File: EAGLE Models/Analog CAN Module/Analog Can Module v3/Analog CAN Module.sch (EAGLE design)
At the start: 241 parts, among them IC1 AT90CAN128, IC2 MCP2551SO8, IC3 NUP2105L, IC5 FT232RL, Q1 56P2859, U1 LTC2053, U10 LTC2053, U11 LTC2053, U12 LTC2053, U13 LTC2053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

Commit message: Added CC resistors
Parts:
- removed R12: (no value), rcl:R-US_R0603
- added R11, R84, R85, R86, R87, R88, R89, R90, R91, R92, R93, R94, R95, R96, R97, R98: (no value), rcl:R-US_R0603
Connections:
- new net A10CC: D17.C, R90.2
- new net A11CC: D18.C, R88.2
- new net A12CC: D11.C, R11.2
- new net A13CC: D12.C, R84.2
- new net A14CC: D13.C, R85.2
- new net A15CC: D14.C, R86.2
- new net A16CC: D15.C, R87.2
- new net A17CC: D26.C, R91.2
- new net A18CC: D25.C, R92.2
- new net A19CC: D23.C, R93.2
- new net A20CC: D24.C, R94.2
- new net A21CC: D19.C, R98.2
- new net A22CC: D20.C, R97.2
- new net A23CC: D21.C, R96.2
- new net A24CC: D22.C, R95.2
- new net A9CC: D16.C, R89.2
- net A10: now also R90.1; no longer D17.C
- net A11: now also R88.1; no longer D18.C
- net A12: now also R11.1; no longer D11.C
- net A13: now also R84.1; no longer D12.C
- net A14: now also R85.1; no longer D13.C
- net A15: now also R86.1; no longer D14.C
- net A16: now also R87.1; no longer D15.C
- net A17: now also R91.1; no longer D26.C
- net A18: now also R92.1; no longer D25.C
- net A19: now also R93.1; no longer D23.C
- net A20: now also R94.1; no longer D24.C
- net A21: now also R98.1; no longer D19.C
- net A22: now also R97.1; no longer D20.C
- net A23: now also R96.1; no longer D21.C
- net A24: now also R95.1; no longer D22.C
- net A8: no longer R12.1
- net A8CC: no longer R12.2
- net A9: now also R89.1; no longer D16.C
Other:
- moved on the sheet: D19

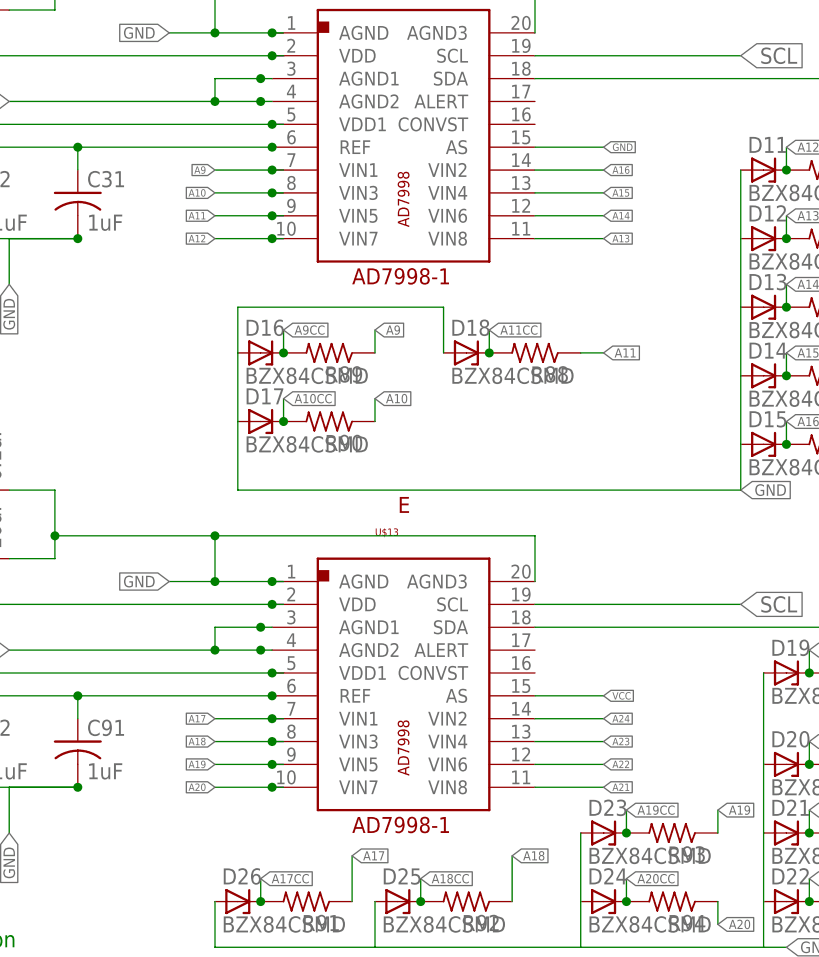
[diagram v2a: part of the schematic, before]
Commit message: Corrected ADC imputs
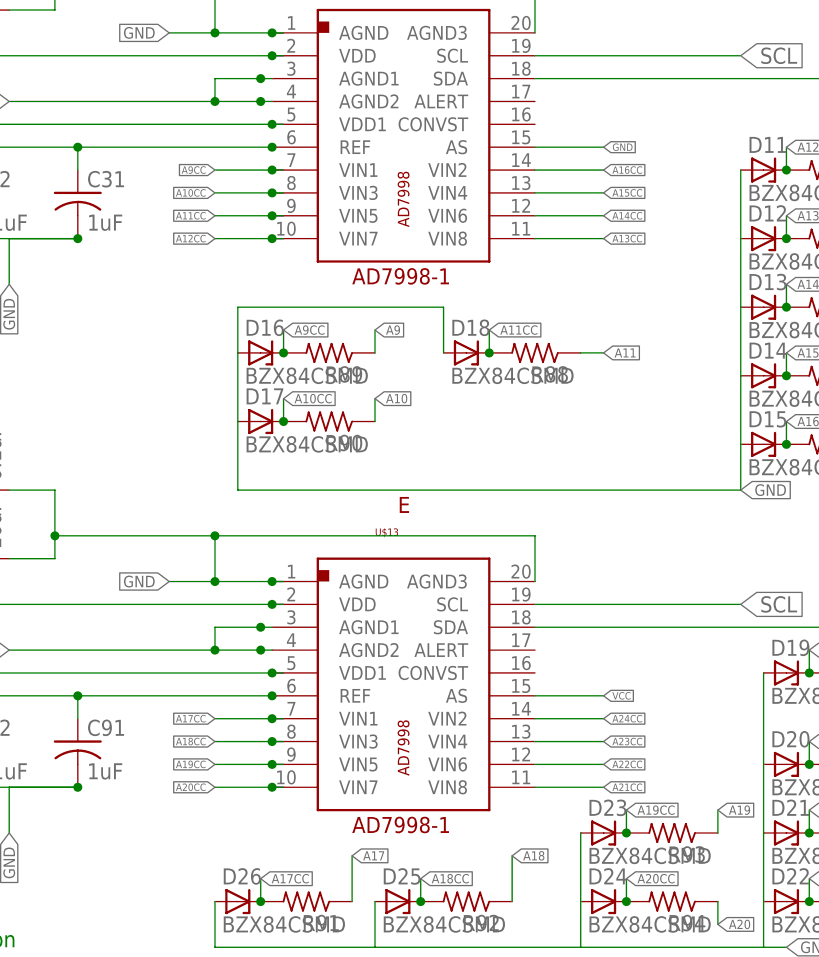
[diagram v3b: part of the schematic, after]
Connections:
- net A10: no longer U$9.VIN3
- net A10CC: now also U$9.VIN3
- net A11: no longer U$9.VIN5
- net A11CC: now also U$9.VIN5
- net A12: no longer U$9.VIN7
- net A12CC: now also U$9.VIN7
- net A13: no longer U$9.VIN8
- net A13CC: now also U$9.VIN8
- net A14: no longer U$9.VIN6
- net A14CC: now also U$9.VIN6
- net A15: no longer U$9.VIN4
- net A15CC: now also U$9.VIN4
- net A16: no longer U$9.VIN2
- net A16CC: now also U$9.VIN2
- net A17: no longer U$13.VIN1
- net A17CC: now also U$13.VIN1
- net A18: no longer U$13.VIN3
- net A18CC: now also U$13.VIN3
- net A19: no longer U$13.VIN5
- net A19CC: now also U$13.VIN5
- net A20: no longer U$13.VIN7
- net A20CC: now also U$13.VIN7
- net A21: no longer U$13.VIN8
- net A21CC: now also U$13.VIN8
- net A22: no longer U$13.VIN6
- net A22CC: now also U$13.VIN6
- net A23: no longer U$13.VIN4
- net A23CC: now also U$13.VIN4
- net A24: no longer U$13.VIN2
- net A24CC: now also U$13.VIN2
- net A9: no longer U$9.VIN1
- net A9CC: now also U$9.VIN1

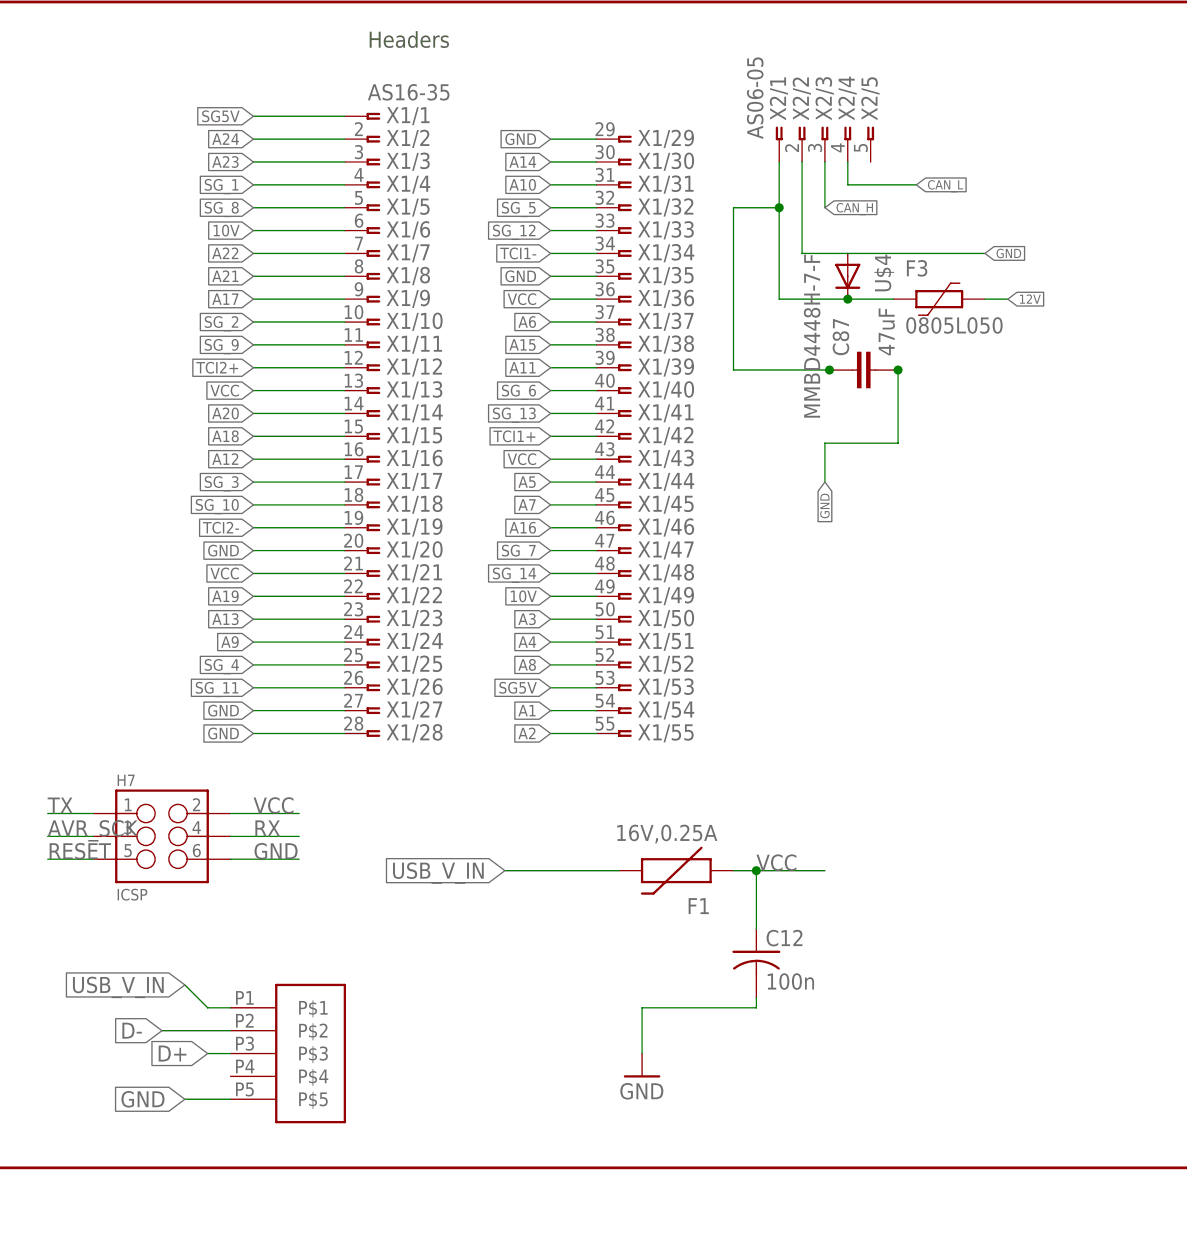
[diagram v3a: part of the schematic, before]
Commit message: Updated decoupling cap circuit, added more gnd vias
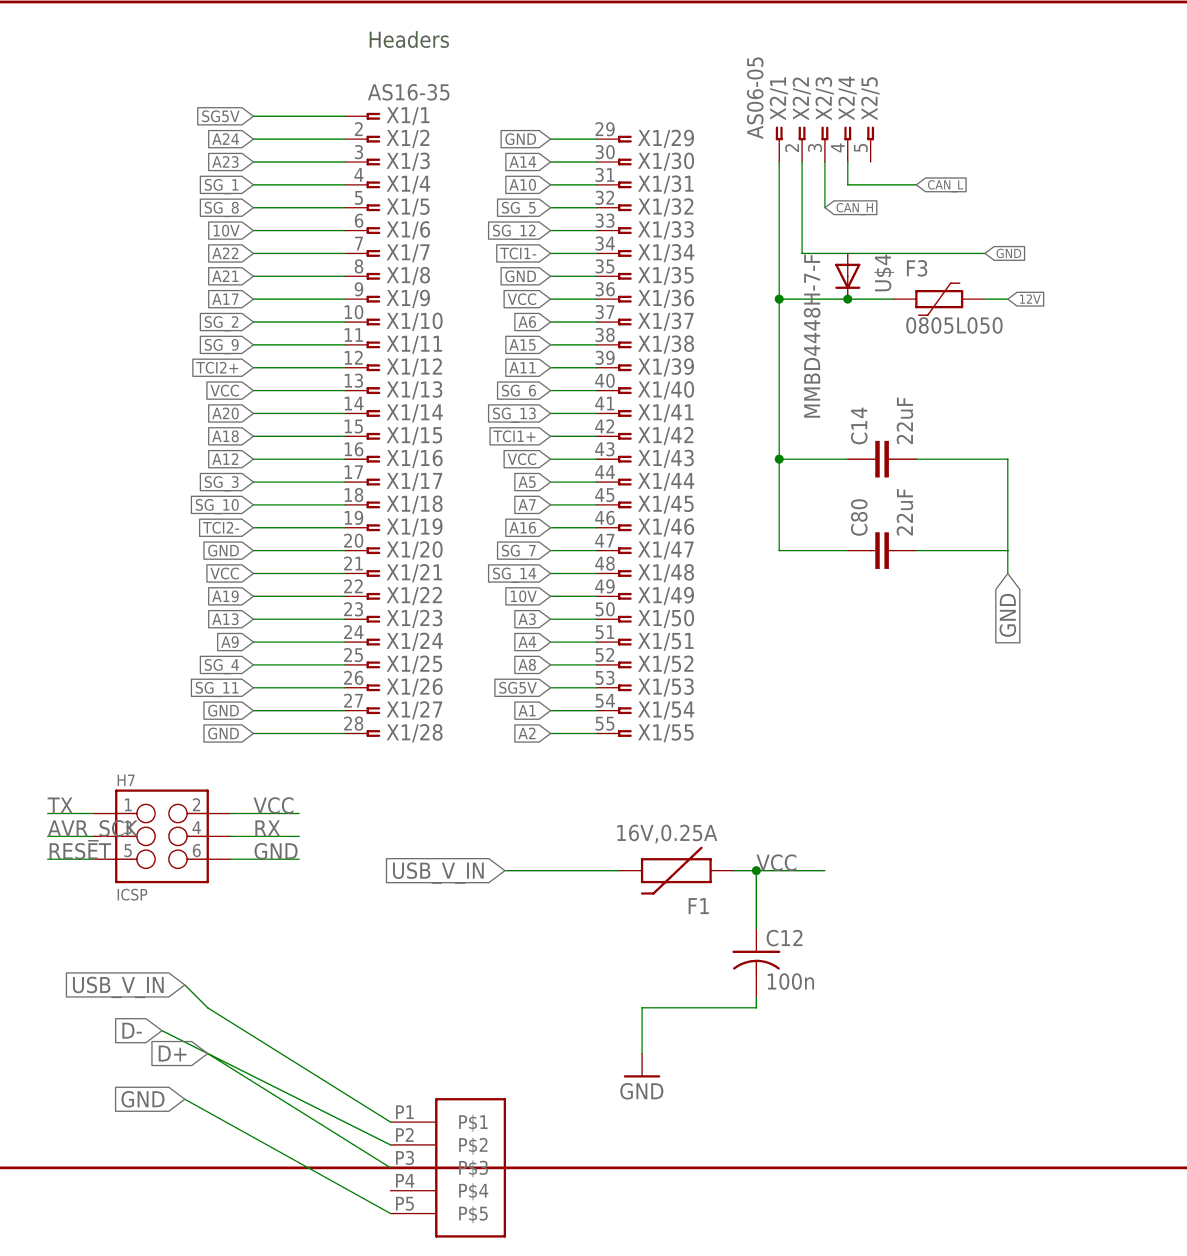
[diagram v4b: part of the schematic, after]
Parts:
- removed C87: 47uF, rcl:C-EUC0805
- added C14, C80: 22uF, rcl:C-EUC0805
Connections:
- net 12V_PREPTC: now also C14.1, C80.1; no longer C87.1
- net GND: now also C14.2, C80.2; no longer C87.2
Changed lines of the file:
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@@
 <part name="D25" library="diode" deviceset="BZX84CSMD" device=""/>
 <part name="D26" library="diode" deviceset="BZX84CSMD" device=""/>
-<part name="C87" library="rcl" deviceset="C-EU" device="C0805" value="47uF"/>
 <part name="U$4" library="diodes-inc" deviceset="MMBD4448H-7-F" device=""/>
 <part name="F3" library="LittleFuse" deviceset="?" device="0805L" technology="050"/>
@@
 <part name="R98" library="rcl" deviceset="R-US_" device="R0603"/>
 <part name="R11" library="rcl" deviceset="R-US_" device="R0603"/>
+<part name="C14" library="rcl" deviceset="C-EU" device="C0805" value="22uF"/>
+<part name="C80" library="rcl" deviceset="C-EU" device="C0805" value="22uF"/>
 </parts>
 <sheets>
@@
 <instance part="D25" gate="G$1" x="91.44" y="-91.44"/>
 <instance part="D26" gate="G$1" x="73.66" y="-91.44"/>
-<instance part="C87" gate="G$1" x="112.268" y="-152.654" rot="R90"/>
 <instance part="U$4" gate="G$1" x="111.76" y="-142.24" rot="R270"/>
 <instance part="F3" gate="G$1" x="121.92" y="-144.78"/>
@@
 <instance part="R98" gate="G$1" x="142.24" y="-66.04" rot="R180"/>
 <instance part="R11" gate="G$1" x="139.7" y="-10.16" rot="R180"/>
+<instance part="C14" gate="G$1" x="114.3" y="-162.56" rot="R90"/>
+<instance part="C80" gate="G$1" x="114.3" y="-172.72" rot="R90"/>
 </instances>
 <busses>
@@
 <segment>
 <pinref part="U$14" gate="G$1" pin="P$5"/>
-<wire x1="43.18" y1="-233.68" x2="38.1" y2="-233.68" width="0.1524" layer="91"/>
+<wire x1="60.96" y1="-246.38" x2="38.1" y2="-233.68" width="0.1524" layer="91"/>
 <label x="38.1" y="-233.68" size="1.778" layer="95" rot="R180" xref="yes"/>
 </segment>
@@
 </segment>
 <segment>
-<label x="109.22" y="-165.1" size="1.016" layer="95" rot="R270" xref="yes"/>
-<pinref part="C87" gate="G$1" pin="2"/>
-<wire x1="109.22" y1="-160.782" x2="109.22" y2="-165.1" width="0.1524" layer="91"/>
-<wire x1="117.348" y1="-152.654" x2="117.348" y2="-160.782" width="0.1524" layer="91"/>
-<wire x1="117.348" y1="-160.782" x2="109.22" y2="-160.782" width="0.1524" layer="91"/>
-<junction x="117.348" y="-152.654"/>
-</segment>
-<segment>
 <pinref part="D3" gate="G$1" pin="A"/>
 <wire x1="58.42" y1="27.94" x2="53.34" y2="27.94" width="0.1524" layer="91"/>
@@
 <label x="127" y="-139.7" size="1.016" layer="95" xref="yes"/>
 </segment>
+<segment>
+<pinref part="C80" gate="G$1" pin="2"/>
+<wire x1="119.38" y1="-172.72" x2="129.54" y2="-172.72" width="0.1524" layer="91"/>
+<label x="129.54" y="-175.26" size="1.778" layer="95" rot="R270" xref="yes"/>
+<pinref part="C14" gate="G$1" pin="2"/>
+<wire x1="119.38" y1="-162.56" x2="129.54" y2="-162.56" width="0.1524" layer="91"/>
+<wire x1="129.54" y1="-162.56" x2="129.54" y2="-172.72" width="0.1524" layer="91"/>
+<wire x1="129.54" y1="-175.26" x2="129.54" y2="-172.72" width="0.1524" layer="91"/>
+</segment>
 </net>
 <net name="XTAL1" class="0">
@@
 <segment>
 <pinref part="U$14" gate="G$1" pin="P$2"/>
-<wire x1="43.18" y1="-226.06" x2="35.56" y2="-226.06" width="0.1524" layer="91"/>
+<wire x1="60.96" y1="-238.76" x2="35.56" y2="-226.06" width="0.1524" layer="91"/>
 <label x="35.56" y="-226.06" size="1.778" layer="95" rot="R180" xref="yes"/>
 </segment>
@@
 <segment>
 <pinref part="U$14" gate="G$1" pin="P$3"/>
-<wire x1="43.18" y1="-228.6" x2="40.64" y2="-228.6" width="0.1524" layer="91"/>
+<wire x1="60.96" y1="-241.3" x2="40.64" y2="-228.6" width="0.1524" layer="91"/>
 <label x="40.64" y="-228.6" size="1.778" layer="95" rot="R180" xref="yes"/>
 </segment>
@@
 <segment>
 <pinref part="U$14" gate="G$1" pin="P$1"/>
-<wire x1="43.18" y1="-223.52" x2="40.64" y2="-223.52" width="0.1524" layer="91"/>
+<wire x1="60.96" y1="-236.22" x2="40.64" y2="-223.52" width="0.1524" layer="91"/>
 <wire x1="40.64" y1="-223.52" x2="38.1" y2="-220.98" width="0.1524" layer="91"/>
 <label x="38.1" y="-220.98" size="1.778" layer="95" rot="R180" xref="yes"/>
@@
 <segment>
 <pinref part="X2" gate="/1" pin="1"/>
-<wire x1="104.14" y1="-129.54" x2="104.14" y2="-134.62" width="0.1524" layer="91"/>
-<wire x1="99.06" y1="-152.654" x2="99.06" y2="-134.62" width="0.1524" layer="91"/>
-<wire x1="99.06" y1="-134.62" x2="104.14" y2="-134.62" width="0.1524" layer="91"/>
-<junction x="104.14" y="-134.62"/>
-<wire x1="109.982" y1="-152.654" x2="109.728" y2="-152.654" width="0.1524" layer="91"/>
-<pinref part="C87" gate="G$1" pin="1"/>
-<junction x="109.728" y="-152.654"/>
-<wire x1="109.728" y1="-152.654" x2="99.06" y2="-152.654" width="0.1524" layer="91"/>
-<wire x1="104.14" y1="-134.62" x2="104.14" y2="-144.78" width="0.1524" layer="91"/>
+<wire x1="104.14" y1="-129.54" x2="104.14" y2="-144.78" width="0.1524" layer="91"/>
 <pinref part="F3" gate="G$1" pin="2"/>
 <wire x1="116.84" y1="-144.78" x2="111.76" y2="-144.78" width="0.1524" layer="91"/>
@@
 <wire x1="111.76" y1="-144.78" x2="104.14" y2="-144.78" width="0.1524" layer="91"/>
 <junction x="111.76" y="-144.78"/>
+<junction x="104.14" y="-144.78"/>
+<wire x1="104.14" y1="-144.78" x2="104.14" y2="-162.56" width="0.1524" layer="91"/>
+<pinref part="C14" gate="G$1" pin="1"/>
+<wire x1="104.14" y1="-162.56" x2="104.14" y2="-172.72" width="0.1524" layer="91"/>
+<wire x1="111.76" y1="-162.56" x2="104.14" y2="-162.56" width="0.1524" layer="91"/>
+<junction x="104.14" y="-162.56"/>
+<pinref part="C80" gate="G$1" pin="1"/>
+<wire x1="111.76" y1="-172.72" x2="104.14" y2="-172.72" width="0.1524" layer="91"/>
 </segment>
 </net>
